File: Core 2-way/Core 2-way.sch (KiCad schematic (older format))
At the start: 8 parts

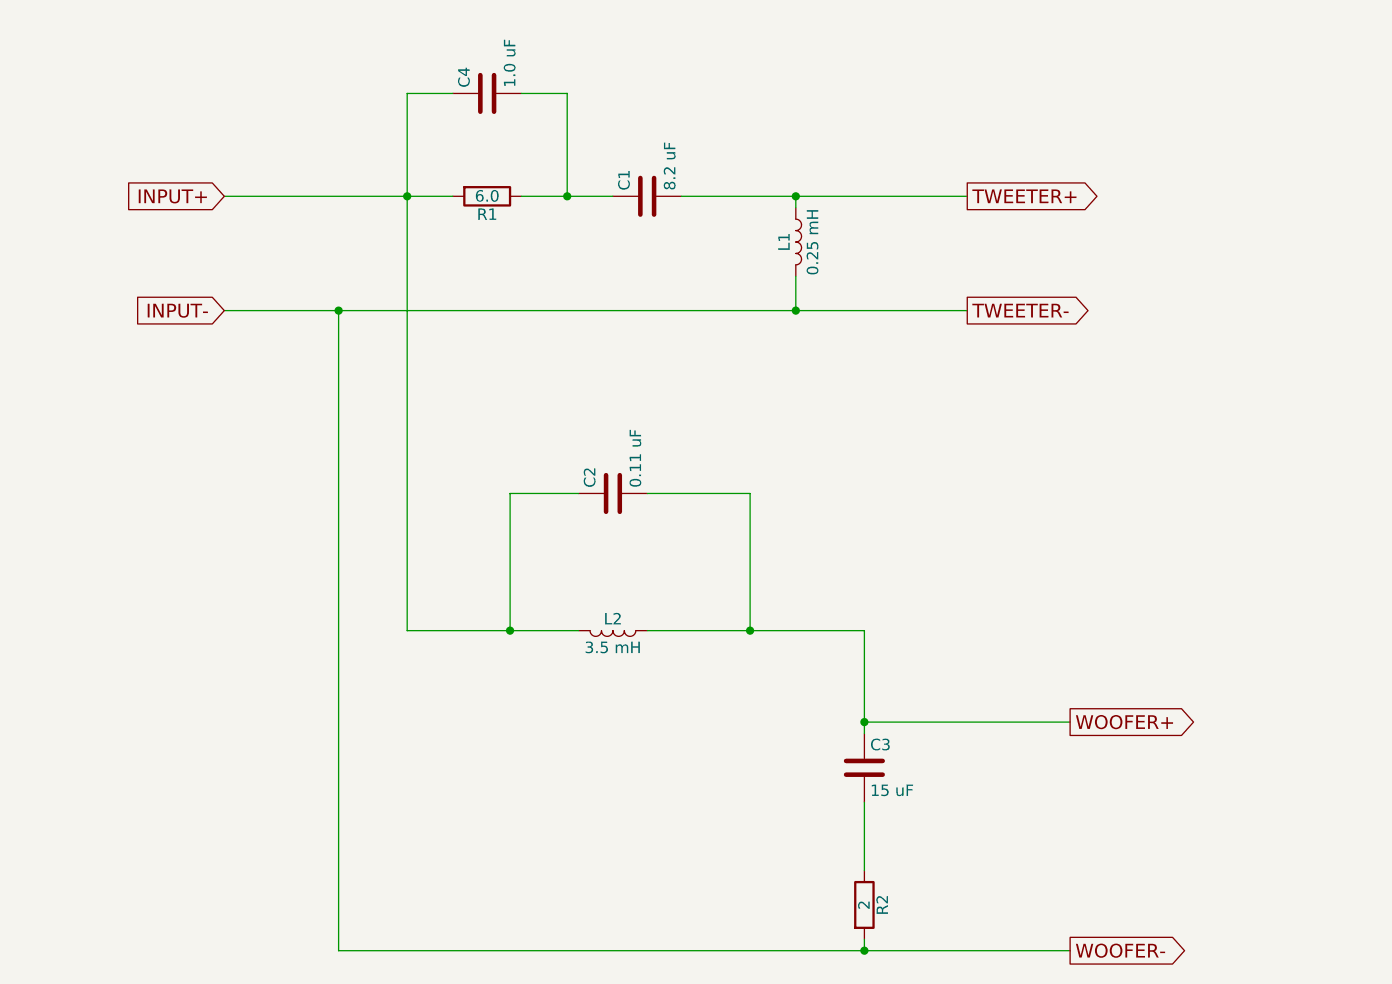
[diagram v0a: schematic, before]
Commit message: feat: Update schematic
 - Replace global labels with connectors
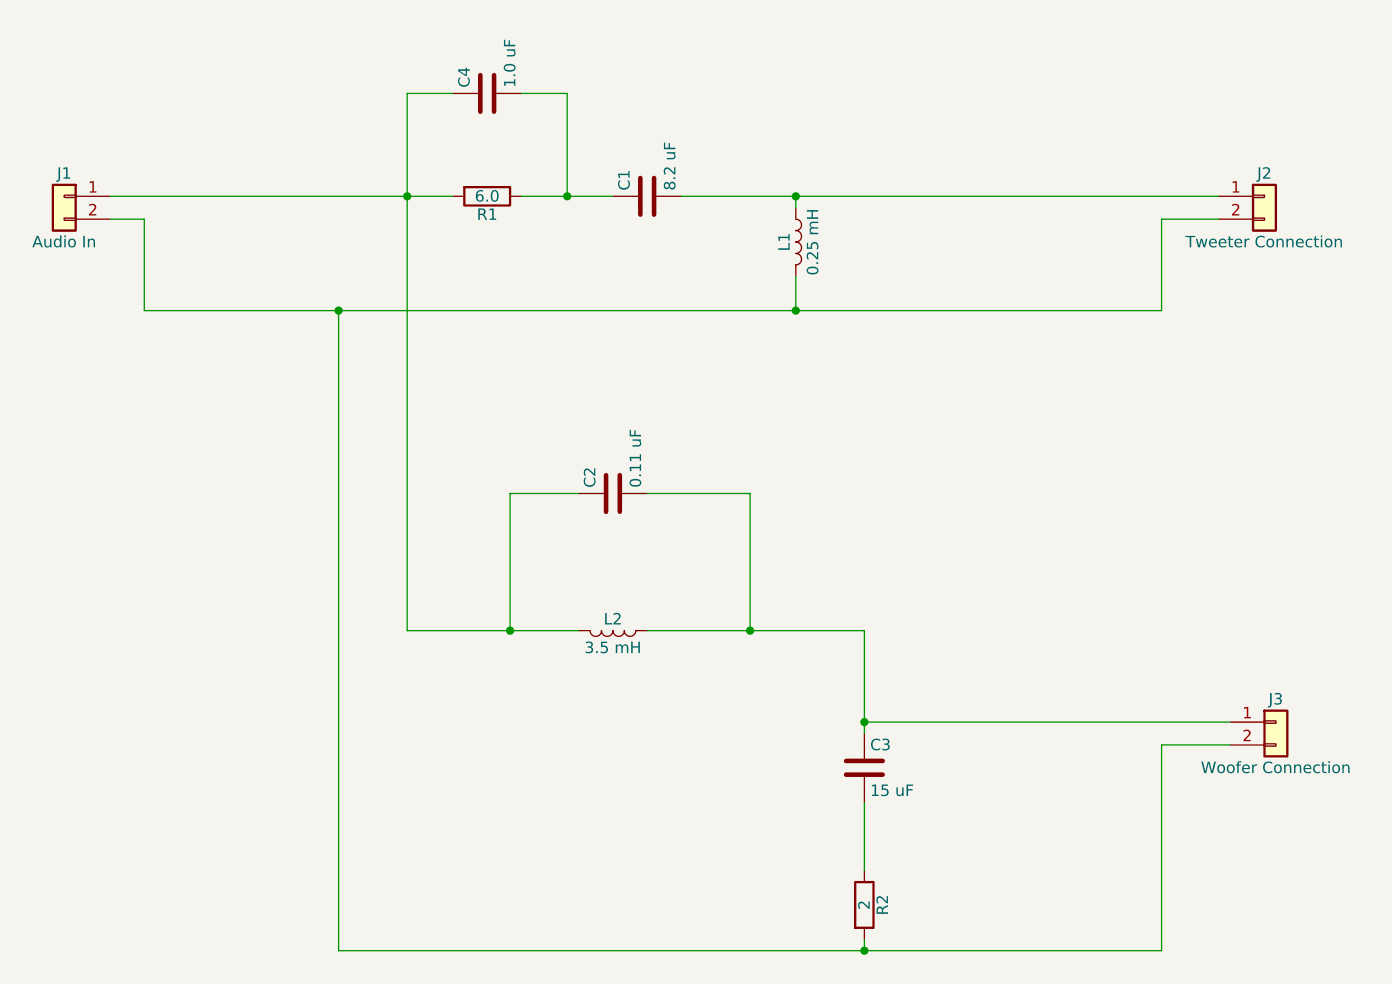
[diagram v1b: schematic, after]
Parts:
- added J1: Audio In, symbol Conn_01x02
- added J2: Tweeter Connection, symbol Conn_01x02
- added J3: Woofer Connection, symbol Conn_01x02
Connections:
- net INPUT+: no longer names the net of C2.1, C4.1, L2.2, R1.2
- net INPUT+: now also J1.1 (Pin_1)
- net INPUT-: no longer names the net of L1.2, R2.2
- net INPUT-: now also J1.2 (Pin_2), J2.2 (Pin_2), J3.2 (Pin_2)
- net TWEETER+: no longer names the net of C1.2, L1.1
- net TWEETER+: now also J2.1 (Pin_1)
- net WOOFER+: no longer names the net of C2.2, C3.1, L2.1
- net WOOFER+: now also J3.1 (Pin_1)
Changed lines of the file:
@@
 LIBS:contrib
 LIBS:valves
+LIBS:Core 2-way-cache
 EELAYER 25 0
 EELAYER END
@@
 	0    1    1    0
 $EndComp
-Text GLabel 1600 2100 0    60   Input ~ 0
-INPUT+
-Text GLabel 1600 2600 0    60   Input ~ 0
-INPUT-
-Text GLabel 4850 2100 2    60   Output ~ 0
-TWEETER+
-Text GLabel 4850 2600 2    60   Output ~ 0
-TWEETER-
-Text GLabel 5300 4400 2    60   Output ~ 0
-WOOFER+
-Text GLabel 5300 5400 2    60   Output ~ 0
-WOOFER-
 Connection ~ 4100 2600
 Wire Wire Line
@@
 	4400 5350 4400 5400
 Wire Wire Line
-	1600 2600 4850 2600
+	1250 2600 5700 2600
 Wire Wire Line
 	2100 5400 2100 2600
 Wire Wire Line
-	5300 5400 2100 5400
+	2100 5400 5700 5400
 Connection ~ 4400 4400
 Wire Wire Line
-	4400 4400 5300 4400
+	4400 4400 6000 4400
 Connection ~ 3900 4000
 Wire Wire Line
@@
 	4100 2150 4100 2100
 Wire Wire Line
-	3600 2100 4850 2100
+	3600 2100 5950 2100
 Connection ~ 3100 2100
 Wire Wire Line
@@
 	2600 1650 2400 1650
 Wire Wire Line
-	1600 2100 2600 2100
+	1100 2100 2600 2100
 Wire Wire Line
 	4400 4750 4400 5050
+$Comp
+L Conn_01x02 J2
+U 1 1 5A3553A6
+P 6150 2100
+F 0 "J2" H 6150 2200 50  0000 C CNN
+F 1 "Tweeter Connection" H 6150 1900 50  0000 C CNN
+F 2 "" H 6150 2100 50  0001 C CNN
+F 3 "" H 6150 2100 50  0001 C CNN
+	1    6150 2100
+	1    0    0    -1
+$EndComp
+$Comp
+L Conn_01x02 J3
+U 1 1 5A355487
+P 6200 4400
+F 0 "J3" H 6200 4500 50  0000 C CNN
+F 1 "Woofer Connection" H 6200 4200 50  0000 C CNN
+F 2 "" H 6200 4400 50  0001 C CNN
+F 3 "" H 6200 4400 50  0001 C CNN
+	1    6200 4400
+	1    0    0    -1
+$EndComp
+$Comp
+L Conn_01x02 J1
+U 1 1 5A3555A6
+P 900 2100
+F 0 "J1" H 900 2200 50  0000 C CNN
+F 1 "Audio In" H 900 1900 50  0000 C CNN
+F 2 "" H 900 2100 50  0001 C CNN
+F 3 "" H 900 2100 50  0001 C CNN
+	1    900  2100
+	-1   0    0    -1
+$EndComp
+Wire Wire Line
+	1100 2200 1250 2200
+Wire Wire Line
+	1250 2200 1250 2600
+Wire Wire Line
+	5950 2200 5700 2200
+Wire Wire Line
+	5700 2200 5700 2600
+Wire Wire Line
+	6000 4500 5700 4500
+Wire Wire Line
+	5700 4500 5700 5400
 $EndSCHEMATC

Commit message: Add component footprints
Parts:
- C1: footprint (none) -> Core-2-Way:DMPC-8.2
- C2: footprint (none) -> Core-2-Way:DMPC-0.10
- C3: footprint (none) -> Core-2-Way:DMPC-15
- C4: footprint (none) -> Core-2-Way:DMPC-1.0
- L1: footprint (none) -> Core-2-Way:255-026
- L2: footprint (none) -> Core-2-Way:255-278
- R1: footprint (none) -> Core-2-Way:MI704
- R2: footprint (none) -> Core-2-Way:MI650
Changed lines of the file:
@@
 LIBS:switches
 LIBS:relays
-LIBS:motors
 LIBS:transistors
 LIBS:conn
@@
 F 0 "R1" V 2830 2100 50  0000 C CNN
 F 1 "6.0" V 2750 2100 50  0000 C CNN
-F 2 "" V 2680 2100 50  0001 C CNN
+F 2 "Core-2-Way:MI704" V 2680 2100 50  0001 C CNN
 F 3 "" H 2750 2100 50  0001 C CNN
 	1    2750 2100
@@
 F 0 "R2" V 4480 5200 50  0000 C CNN
 F 1 "2" V 4400 5200 50  0000 C CNN
-F 2 "" V 4330 5200 50  0001 C CNN
+F 2 "Core-2-Way:MI650" V 4330 5200 50  0001 C CNN
 F 3 "" H 4400 5200 50  0001 C CNN
 	1    4400 5200
@@
 F 0 "C1" H 3475 2200 50  0000 L CNN
 F 1 "8.2 uF" H 3475 2000 50  0000 L CNN
-F 2 "" H 3488 1950 50  0001 C CNN
+F 2 "Core-2-Way:DMPC-8.2" H 3488 1950 50  0001 C CNN
 F 3 "" H 3450 2100 50  0001 C CNN
 	1    3450 2100
@@
 F 0 "C2" H 3325 3500 50  0000 L CNN
 F 1 "0.11 uF" H 3325 3300 50  0000 L CNN
-F 2 "" H 3338 3250 50  0001 C CNN
+F 2 "Core-2-Way:DMPC-0.10" H 3338 3250 50  0001 C CNN
 F 3 "" H 3300 3400 50  0001 C CNN
 	1    3300 3400
@@
 F 0 "C3" H 4425 4700 50  0000 L CNN
 F 1 "15 uF" H 4425 4500 50  0000 L CNN
-F 2 "" H 4438 4450 50  0001 C CNN
+F 2 "Core-2-Way:DMPC-15" H 4438 4450 50  0001 C CNN
 F 3 "" H 4400 4600 50  0001 C CNN
 	1    4400 4600
@@
 F 0 "C4" H 2775 1750 50  0000 L CNN
 F 1 "1.0 uF" H 2775 1550 50  0000 L CNN
-F 2 "" H 2788 1500 50  0001 C CNN
+F 2 "Core-2-Way:DMPC-1.0" H 2788 1500 50  0001 C CNN
 F 3 "" H 2750 1650 50  0001 C CNN
 	1    2750 1650
@@
 F 0 "L1" V 4050 2300 50  0000 C CNN
 F 1 "0.25 mH" V 4175 2300 50  0000 C CNN
-F 2 "" H 4100 2300 50  0001 C CNN
+F 2 "Core-2-Way:255-026" H 4100 2300 50  0001 C CNN
 F 3 "" H 4100 2300 50  0001 C CNN
 	1    4100 2300
@@
 F 0 "L2" V 3250 4000 50  0000 C CNN
 F 1 "3.5 mH" V 3375 4000 50  0000 C CNN
-F 2 "" H 3300 4000 50  0001 C CNN
+F 2 "Core-2-Way:255-278" H 3300 4000 50  0001 C CNN
 F 3 "" H 3300 4000 50  0001 C CNN
 	1    3300 4000

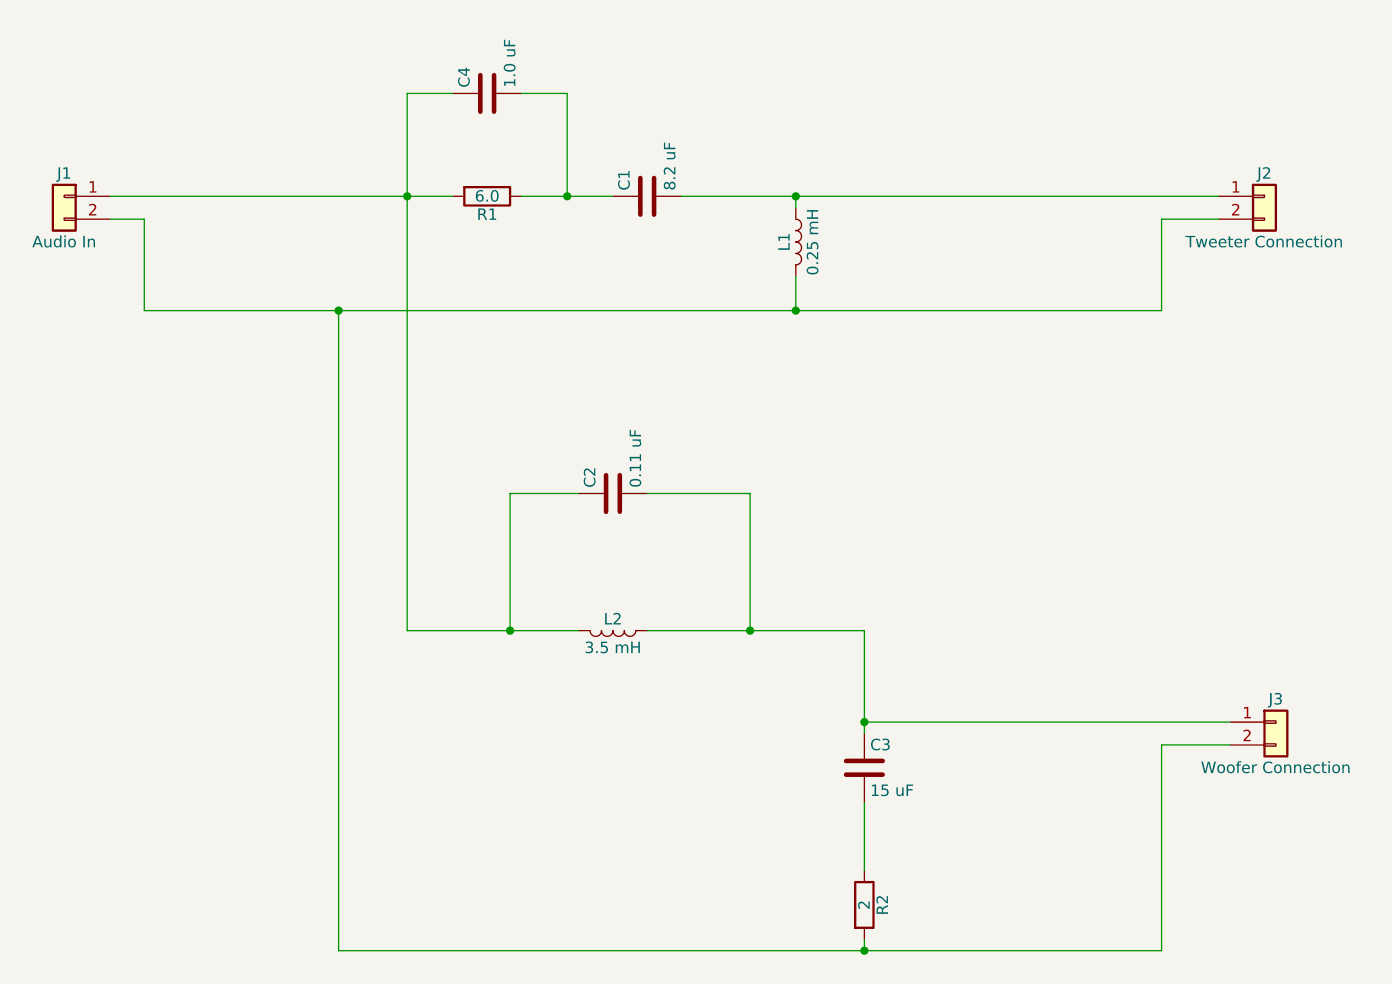
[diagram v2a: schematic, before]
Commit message: Schematic: Rearranged components
Flipped polarity of some components so that the footprint terminal numbers match.
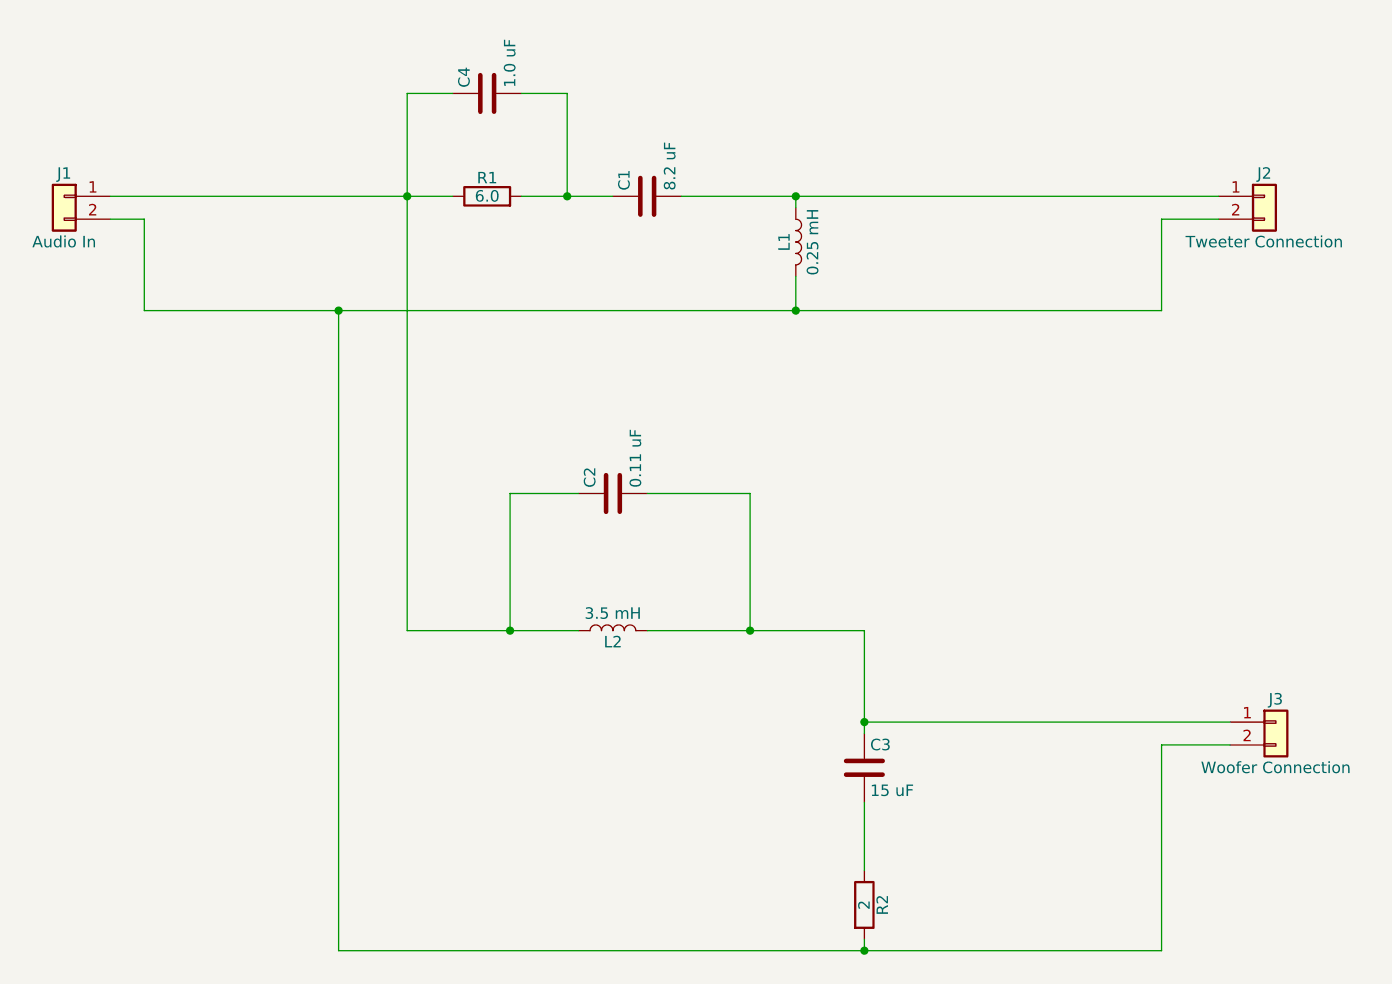
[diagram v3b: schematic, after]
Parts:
- J1, J2, J3: footprint (none) -> Terminal_Blocks:TerminalBlock_Pheonix_PT-3.5mm_2pol
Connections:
- net at C1.1, C4.2: now also R1.2; no longer R1.1
- net at C2.1, C4.1, J1.1 (Pin_1): now also L2.1, R1.1; no longer L2.2, R1.2
- net at C2.2, C3.1, J3.1 (Pin_1): now also L2.2; no longer L2.1
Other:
- moved on the sheet: L2
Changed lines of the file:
@@
 F 3 "" H 2750 2100 50  0001 C CNN
 	1    2750 2100
-	0    1    1    0
+	0    -1   -1   0
 $EndComp
 $Comp
@@
 F 3 "" H 3300 4000 50  0001 C CNN
 	1    3300 4000
-	0    1    1    0
+	0    -1   -1   0
 $EndComp
 Connection ~ 4100 2600
@@
 F 0 "J2" H 6150 2200 50  0000 C CNN
 F 1 "Tweeter Connection" H 6150 1900 50  0000 C CNN
-F 2 "" H 6150 2100 50  0001 C CNN
+F 2 "Terminal_Blocks:TerminalBlock_Pheonix_PT-3.5mm_2pol" H 6150 2100 50  0001 C CNN
 F 3 "" H 6150 2100 50  0001 C CNN
 	1    6150 2100
@@
 F 0 "J3" H 6200 4500 50  0000 C CNN
 F 1 "Woofer Connection" H 6200 4200 50  0000 C CNN
-F 2 "" H 6200 4400 50  0001 C CNN
+F 2 "Terminal_Blocks:TerminalBlock_Pheonix_PT-3.5mm_2pol" H 6200 4400 50  0001 C CNN
 F 3 "" H 6200 4400 50  0001 C CNN
 	1    6200 4400
@@
 F 0 "J1" H 900 2200 50  0000 C CNN
 F 1 "Audio In" H 900 1900 50  0000 C CNN
-F 2 "" H 900 2100 50  0001 C CNN
+F 2 "Terminal_Blocks:TerminalBlock_Pheonix_PT-3.5mm_2pol" H 900 2100 50  0001 C CNN
 F 3 "" H 900 2100 50  0001 C CNN
 	1    900  2100
